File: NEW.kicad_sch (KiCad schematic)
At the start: 21 parts, among them J1 Screw_Terminal_01x16, J2 Screw_Terminal_01x16, J3 buck converter, J4 Infrared, J5 BMI, J6 light sensor, J7 servo, J8 Screw_Terminal_01x03, J9 battery +, Q1 PN2222A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

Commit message: 2.0
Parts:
- removed J5: BMI, Connector_PinHeader_2.00mm:PinHeader_1x07_P2.00mm_Vertical, symbol Connector:Screw_Terminal_01x07
- removed J6: light sensor, Connector_PinHeader_2.00mm:PinHeader_1x05_P2.00mm_Vertical, symbol Connector:Screw_Terminal_01x05
- removed J9: battery +, Connector_PinHeader_2.54mm:PinHeader_1x01_P2.54mm_Vertical, symbol Connector:Screw_Terminal_01x01
- added C4: C_Polarized_Small, Capacitor_THT:C_Disc_D3.8mm_W2.6mm_P2.50mm, symbol Device:C_Polarized_Small
- added J10: boost conv (IN), TerminalBlock:TerminalBlock_Altech_AK300-2_P5.00mm, symbol Connector:Screw_Terminal_01x02
- added J11: Battery, TerminalBlock:TerminalBlock_Altech_AK300-2_P5.00mm, symbol Connector:Screw_Terminal_01x02
- added J5: Light Sensor, Connector_PinHeader_2.54mm:PinHeader_1x04_P2.54mm_Vertical, symbol Connector:Screw_Terminal_01x04
- added J6: CAM UART, Connector_PinHeader_2.54mm:PinHeader_1x03_P2.54mm_Vertical, symbol Connector:Screw_Terminal_01x03
- added J9: BMI, Connector_PinHeader_2.54mm:PinHeader_1x04_P2.54mm_Vertical, symbol Connector:Screw_Terminal_01x04
- D1: footprint Connector_PinHeader_2.54mm:PinHeader_1x02_P2.54mm_Vertical -> LED_THT:LED_D5.0mm
- J3: value buck converter -> boost conv (OUT); footprint Connector_PinHeader_2.54mm:PinHeader_1x02_P2.54mm_Vertical -> TerminalBlock:TerminalBlock_Altech_AK300-2_P5.00mm
- Q1: footprint Package_TO_SOT_THT:TO-92_Inline -> Package_TO_SOT_THT:TO-92_Inline_Wide
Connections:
- net GND: now also D1.1 (K), C4.2, J10.2 (Pin_2), J11.2 (Pin_2); no longer R5.1
- net at J1.16 (Pin_16), J4.2 (Pin_2): now also C4.1, J10.1 (Pin_1), J11.1 (Pin_1)
- net at J1.3 (Pin_3), J4.3 (Pin_3): now also R5.2; no longer D1.2 (A)
- net at U2.GND1: now also J6.3 (Pin_3)
- net at U2.U0R: now also J6.1 (Pin_1)
- net at U2.U0T: now also J6.2 (Pin_2)
- net at J2.3 (Pin_3): now also J5.4 (Pin_4), J9.1 (Pin_1)
- net at J2.4 (Pin_4): now also J5.3 (Pin_3), J9.2 (Pin_2)
- net at J2.5 (Pin_5): now also J5.2 (Pin_2), J9.3 (Pin_3)
- net at J2.6 (Pin_6): now also J5.1 (Pin_1), J9.4 (Pin_4)
- new net: D1.2 (A), R5.1
- no-connect marks 35 -> 28

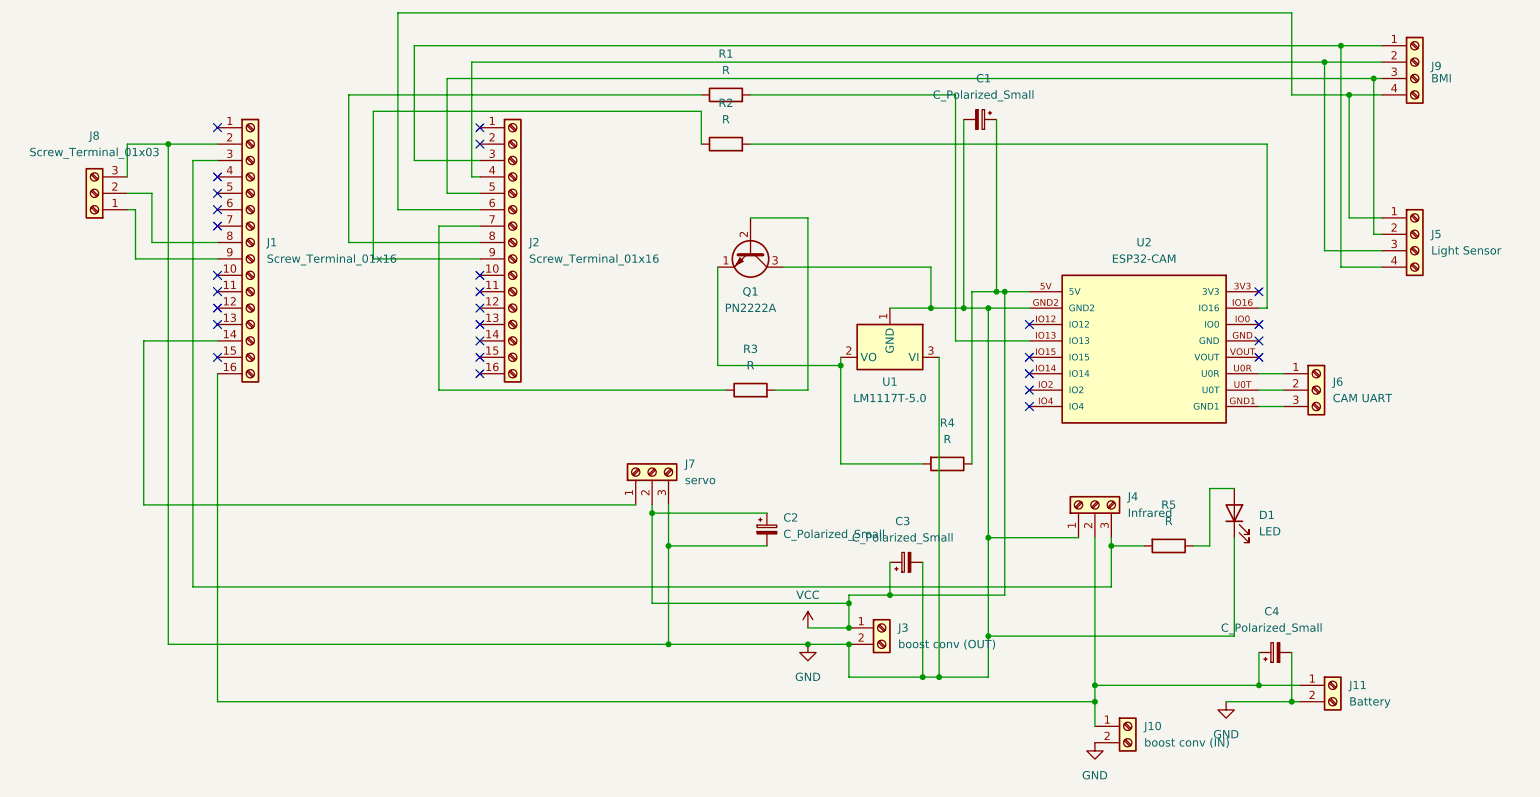
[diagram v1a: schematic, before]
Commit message: fixed proper wiring on power
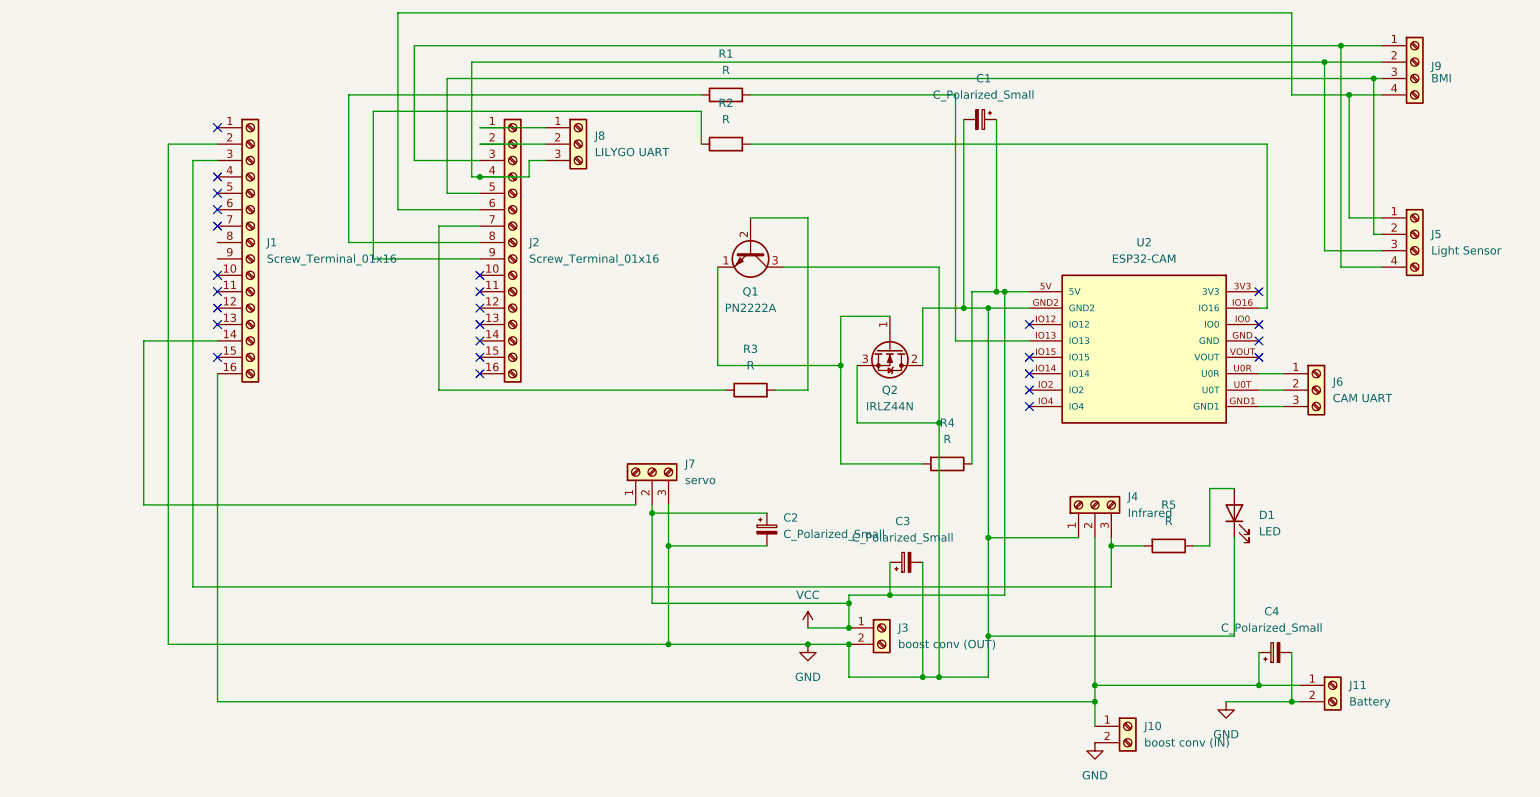
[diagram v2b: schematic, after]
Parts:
- removed U1: LM1117T-5.0, Package_TO_SOT_THT:TO-220-3_Horizontal_TabDown, symbol Regulator_Linear:LM1117T-5.0
- added Q2: IRLZ44N, Package_TO_SOT_THT:TO-220-3_Vertical, symbol Transistor_FET:IRLZ44N
- J8: value Screw_Terminal_01x03 -> LILYGO UART
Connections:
- net GND: now also Q2.2 (D), Q2.3 (S); no longer J8.3 (Pin_3)
- net at J2.4 (Pin_4), J5.3 (Pin_3), J9.2 (Pin_2): now also J8.3 (Pin_3)
- net at Q1.1 (E), R4.2: now also Q2.1 (G)
- net at J1.8 (Pin_8): no longer J8.2 (Pin_2)
- net at J1.9 (Pin_9): no longer J8.1 (Pin_1)
- net at J2.1 (Pin_1): now also J8.1 (Pin_1)
- net at J2.2 (Pin_2): now also J8.2 (Pin_2)
- no-connect marks 28 -> 26
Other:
- moved on the sheet: J8

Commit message: final rev
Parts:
- added D2: 1N4007, Diode_THT:D_DO-41_SOD81_P12.70mm_Horizontal, symbol Diode:1N4007
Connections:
- net GND: now also D2.2 (A); no longer C1.2, Q2.2 (D), U2.GND2
- net VCC: now also D2.1 (K)
- new net: C1.2, Q2.2 (D), U2.GND2
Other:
- moved on the sheet: R4
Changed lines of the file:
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@@
+	)
+	(junction
+		(at 128.27 125.73)
+		(diameter 0)
+		(color 0 0 0 0)
 	)
 	(junction
@@
 	)
 	(junction
-		(at 173.99 121.92)
-		(diameter 0)
-		(color 0 0 0 0)
-	)
-	(junction
 		(at 121.92 118.11)
 		(diameter 0)
@@
 	)
 	(junction
+		(at 187.96 137.16)
+		(diameter 0)
+		(color 0 0 0 0)
+	)
+	(junction
 		(at 95.25 66.04)
 		(diameter 0)
@@
 	)
 	(junction
+		(at 128.27 118.11)
+		(diameter 0)
+		(color 0 0 0 0)
+	)
+	(junction
 		(at 229.87 53.34)
 		(diameter 0)
@@
 	)
 	(junction
-		(at 173.99 137.16)
+		(at 124.46 125.73)
 		(diameter 0)
 		(color 0 0 0 0)
@@
 	)
 	(junction
-		(at 173.99 86.36)
-		(diameter 0)
-		(color 0 0 0 0)
-	)
-	(junction
 		(at 152.4 132.08)
-		(diameter 0)
-		(color 0 0 0 0)
-	)
-	(junction
-		(at 124.46 123.19)
 		(diameter 0)
 		(color 0 0 0 0)
@@
 	(wire
 		(pts
-			(xy 124.46 123.19) (xy 139.7 123.19)
+			(xy 124.46 125.73) (xy 128.27 125.73)
 		)
 		(stroke
@@
 	(wire
 		(pts
+			(xy 124.46 125.73) (xy 124.46 138.43)
+		)
+		(stroke
+			(width 0)
+			(type default)
+		)
+	)
+	(wire
+		(pts
 			(xy 166.37 143.51) (xy 173.99 143.51)
 		)
@@
 	(wire
 		(pts
-			(xy 173.99 121.92) (xy 187.96 121.92)
-		)
-		(stroke
-			(width 0)
-			(type default)
-		)
-	)
-	(wire
-		(pts
 			(xy 95.25 78.74) (xy 78.74 78.74)
 		)
@@
 	(wire
 		(pts
+			(xy 128.27 125.73) (xy 139.7 125.73)
+		)
+		(stroke
+			(width 0)
+			(type default)
+		)
+	)
+	(wire
+		(pts
 			(xy 133.35 99.06) (xy 88.9 99.06)
 		)
@@
 	(wire
 		(pts
-			(xy 171.45 110.49) (xy 171.45 83.82)
+			(xy 172.72 110.49) (xy 172.72 83.82)
 		)
 		(stroke
@@
 	(wire
 		(pts
-			(xy 151.13 110.49) (xy 163.83 110.49)
+			(xy 151.13 110.49) (xy 157.48 110.49)
 		)
 		(stroke
@@
 	(wire
 		(pts
-			(xy 173.99 86.36) (xy 180.34 86.36)
+			(xy 170.18 86.36) (xy 180.34 86.36)
 		)
 		(stroke
@@
 	(wire
 		(pts
-			(xy 124.46 116.84) (xy 124.46 123.19)
-		)
-		(stroke
-			(width 0)
-			(type default)
-		)
-	)
-	(wire
-		(pts
-			(xy 173.99 121.92) (xy 173.99 86.36)
-		)
-		(stroke
-			(width 0)
-			(type default)
-		)
-	)
-	(wire
-		(pts
-			(xy 121.92 118.11) (xy 139.7 118.11)
+			(xy 128.27 118.11) (xy 139.7 118.11)
+		)
+		(stroke
+			(width 0)
+			(type default)
+		)
+	)
+	(wire
+		(pts
+			(xy 121.92 118.11) (xy 128.27 118.11)
 		)
 		(stroke
@@
 	(wire
 		(pts
-			(xy 124.46 123.19) (xy 124.46 138.43)
-		)
-		(stroke
-			(width 0)
-			(type default)
-		)
-	)
-	(wire
-		(pts
-			(xy 170.18 86.36) (xy 173.99 86.36)
-		)
-		(stroke
-			(width 0)
-			(type default)
-		)
-	)
-	(wire
-		(pts
 			(xy 234.95 48.26) (xy 226.06 48.26)
 		)
@@
 	(wire
 		(pts
-			(xy 171.45 83.82) (xy 175.26 83.82)
+			(xy 172.72 83.82) (xy 175.26 83.82)
 		)
 		(stroke
@@
 	(wire
 		(pts
-			(xy 173.99 137.16) (xy 212.09 137.16)
+			(xy 173.99 137.16) (xy 187.96 137.16)
 		)
 		(stroke
@@
 	(wire
 		(pts
-			(xy 173.99 137.16) (xy 173.99 121.92)
+			(xy 187.96 137.16) (xy 187.96 121.92)
 		)
 		(stroke
@@
 	(wire
 		(pts
+			(xy 187.96 137.16) (xy 212.09 137.16)
+		)
+		(stroke
+			(width 0)
+			(type default)
+		)
+	)
+	(wire
+		(pts
 			(xy 129.54 55.88) (xy 129.54 60.96)
 		)
@@
 		(pts
 			(xy 43.18 91.44) (xy 43.18 116.84)
+		)
+		(stroke
+			(width 0)
+			(type default)
+		)
+	)
+	(wire
+		(pts
+			(xy 172.72 110.49) (xy 165.1 110.49)
+		)
+		(stroke
+			(width 0)
+			(type default)
+		)
+	)
+	(wire
+		(pts
+			(xy 139.7 125.73) (xy 139.7 123.19)
+		)
+		(stroke
+			(width 0)
+			(type default)
+		)
+	)
+	(wire
+		(pts
+			(xy 124.46 116.84) (xy 124.46 125.73)
 		)
 		(stroke
@@
 	(symbol
 		(lib_id "Device:R")
-		(at 167.64 110.49 270)
+		(at 161.29 110.49 270)
 		(unit 1)
 		(exclude_from_sim no)
@@
 		(fields_autoplaced yes)
 		(property "Reference" "R4"
-			(at 167.64 104.14 90)
+			(at 161.29 104.14 90)
 			(effects
 				(font
@@
 		)
 		(property "Value" "R"
-			(at 167.64 106.68 90)
+			(at 161.29 106.68 90)
 			(effects
 				(font
@@
 		)
 		(property "Footprint" "Resistor_THT:R_Axial_DIN0207_L6.3mm_D2.5mm_P7.62mm_Horizontal"
-			(at 167.64 108.712 90)
+			(at 161.29 108.712 90)
 			(effects
 				(font
@@
 		)
 		(property "Datasheet" "~"
-			(at 167.64 110.49 0)
+			(at 161.29 110.49 0)
 			(effects
 				(font
@@
 		)
 		(property "Description" "Resistor"
-			(at 167.64 110.49 0)
+			(at 161.29 110.49 0)
 			(effects
 				(font
@@
 					(unit 1)
 				)
+			)
+		)
+	)
+	(symbol
+		(lib_id "Diode:1N4007")
+		(at 128.27 121.92 270)
+		(unit 1)
+		(exclude_from_sim no)
+		(in_bom yes)
+		(on_board yes)
+		(dnp no)
+		(fields_autoplaced yes)
+		(property "Reference" "D2"
+			(at 130.81 120.6499 90)
+			(effects
+				(font
+					(size 1.27 1.27)
+				)
+				(justify left)
+			)
+		)
+		(property "Value" "1N4007"
+			(at 130.81 123.1899 90)
+			(effects
+				(font
+					(size 1.27 1.27)
+				)
+				(justify left)
+			)
+		)
+		(property "Footprint" "Diode_THT:D_DO-41_SOD81_P12.70mm_Horizontal"
+			(at 123.825 121.92 0)
+			(effects
+				(font
+					(size 1.27 1.27)
+				)
+				(hide yes)
+			)
+		)
+		(property "Datasheet" "http://www.vishay.com/docs/88503/1n4001.pdf"
+			(at 128.27 121.92 0)
+			(effects
+				(font
+					(size 1.27 1.27)
+				)
+				(hide yes)
+			)
+		)
+		(property "Description" "1000V 1A General Purpose Rectifier Diode, DO-41"
+			(at 128.27 121.92 0)
+			(effects
+				(font
+					(size 1.27 1.27)
+				)
+				(hide yes)
+			)
+		)
+		(property "Sim.Device" "D"
+			(at 128.27 121.92 0)
+			(effects
+				(font
+					(size 1.27 1.27)
+				)
+				(hide yes)
+			)
+		)
+		(property "Sim.Pins" "1=K 2=A"
+			(at 128.27 121.92 0)
+			(effects
+				(font
+					(size 1.27 1.27)
+				)
+				(hide yes)
+			)
+		)
+		(pin "1"
+		)
+		(pin "2"
+		)
+		(instances
+			(project "NEW"
+				(path "/13055492-be3c-45cb-b82e-51800be76b99"
+					(reference "D2")
+					(unit 1)
+				)
